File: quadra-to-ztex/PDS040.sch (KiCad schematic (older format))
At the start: 11 parts, among them IC1 74CB3T16211DGGR, IC2 74CB3T16211DGGR, IC3 74CB3T16211DGGR, IC4 74CB3T16211DGGR, U14 8807-140-170LH

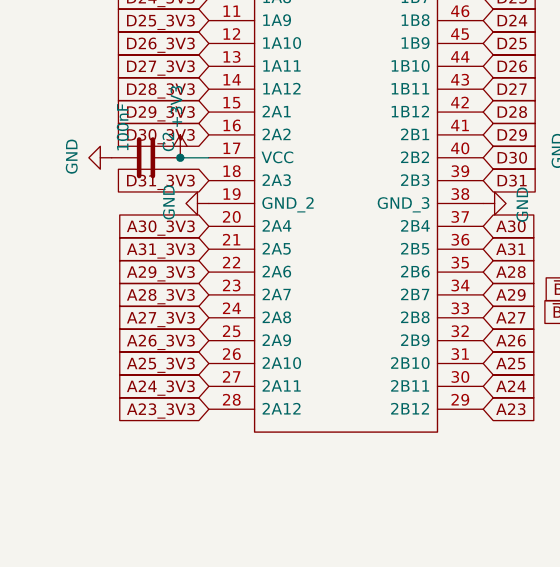
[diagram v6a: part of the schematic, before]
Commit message: fix A18 <-> A19 (hardware)
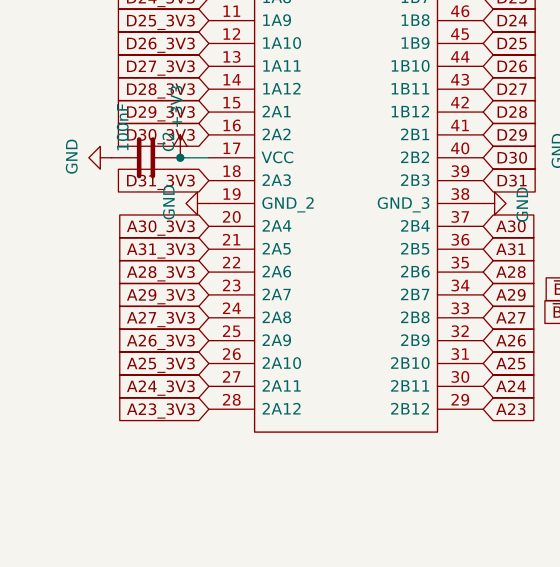
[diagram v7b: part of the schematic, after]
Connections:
- net A28_3V3: now also IC2.22 (2A6); no longer IC2.23 (2A7)
- net A29_3V3: now also IC2.23 (2A7); no longer IC2.22 (2A6)
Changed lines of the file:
@@
 Text GLabel 1000 1900 0    50   Input ~ 0
 A15_3V3
-Text GLabel 1000 6375 0    50   Input ~ 0
+Text GLabel 1000 6275 0    50   Input ~ 0
 A28_3V3
 Text GLabel 1000 6475 0    50   Input ~ 0
@@
 Text GLabel 1000 2400 0    50   Input ~ 0
 A10_3V3
-Text GLabel 1000 6275 0    50   Input ~ 0
+Text GLabel 1000 6375 0    50   Input ~ 0
 A29_3V3
 Text GLabel 1000 6075 0    50   Input ~ 0
@@
 	3125 5250 3125 5350
 $Comp
-L power:GND #PWR?
+L power:GND #PWR0168
 U 1 1 65E4D5E1
 P 3125 4650
-F 0 "#PWR?" H 3125 4400 50  0001 C CNN
+F 0 "#PWR0168" H 3125 4400 50  0001 C CNN
 F 1 "GND" H 3130 4477 50  0000 C CNN
 F 2 "" H 3125 4650 50  0001 C CNN
@@
 Connection ~ 3125 4650
 $Comp
-L power:GND #PWR?
+L power:GND #PWR0169
 U 1 1 65E4D743
 P 3125 4950
-F 0 "#PWR?" H 3125 4700 50  0001 C CNN
+F 0 "#PWR0169" H 3125 4700 50  0001 C CNN
 F 1 "GND" H 3130 4777 50  0000 C CNN
 F 2 "" H 3125 4950 50  0001 C CNN
@@
 Connection ~ 3125 4950
 $Comp
-L power:GND #PWR?
+L power:GND #PWR0170
 U 1 1 65E4D996
 P 3125 5650
-F 0 "#PWR?" H 3125 5400 50  0001 C CNN
+F 0 "#PWR0170" H 3125 5400 50  0001 C CNN
 F 1 "GND" H 3130 5477 50  0000 C CNN
 F 2 "" H 3125 5650 50  0001 C CNN
@@
 $EndComp
 $Comp
-L power:GND #PWR?
+L power:GND #PWR0171
 U 1 1 65E4DC41
 P 3125 5850
-F 0 "#PWR?" H 3125 5600 50  0001 C CNN
+F 0 "#PWR0171" H 3125 5600 50  0001 C CNN
 F 1 "GND" H 3130 5677 50  0000 C CNN
 F 2 "" H 3125 5850 50  0001 C CNN
@@
 $EndComp
 $Comp
-L power:GND #PWR?
+L power:GND #PWR0172
 U 1 1 65E4DEBC
 P 3125 6250
-F 0 "#PWR?" H 3125 6000 50  0001 C CNN
+F 0 "#PWR0172" H 3125 6000 50  0001 C CNN
 F 1 "GND" H 3130 6077 50  0000 C CNN
 F 2 "" H 3125 6250 50  0001 C CNN
@@
 $EndComp
 $Comp
-L power:GND #PWR?
+L power:GND #PWR0173
 U 1 1 65E4E1A4
 P 3125 6550
-F 0 "#PWR?" H 3125 6300 50  0001 C CNN
+F 0 "#PWR0173" H 3125 6300 50  0001 C CNN
 F 1 "GND" H 3130 6377 50  0000 C CNN
 F 2 "" H 3125 6550 50  0001 C CNN
@@
 $EndComp
 $Comp
-L power:GND #PWR?
+L power:GND #PWR0174
 U 1 1 65E4E3F8
 P 3125 6750
-F 0 "#PWR?" H 3125 6500 50  0001 C CNN
+F 0 "#PWR0174" H 3125 6500 50  0001 C CNN
 F 1 "GND" H 3130 6577 50  0000 C CNN
 F 2 "" H 3125 6750 50  0001 C CNN
